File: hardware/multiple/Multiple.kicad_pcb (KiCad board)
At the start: 2 copper layers, 15 x 100 mm, 10 parts, among them J1 AudioJack2_SwitchT, J2 AudioJack2_SwitchT, J3 AudioJack2_SwitchT, J4 AudioJack2_SwitchT, J5 AudioJack2_SwitchT, J6 AudioJack2_SwitchT, J7 AudioJack2_SwitchT, J8 AudioJack2_SwitchT, SW1 SW_Push_DPDT

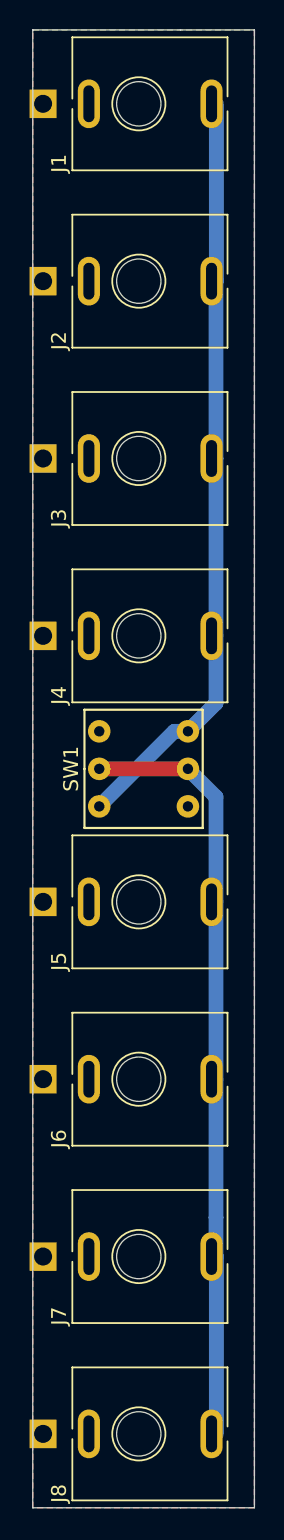
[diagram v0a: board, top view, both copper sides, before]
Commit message: Fix jack centering
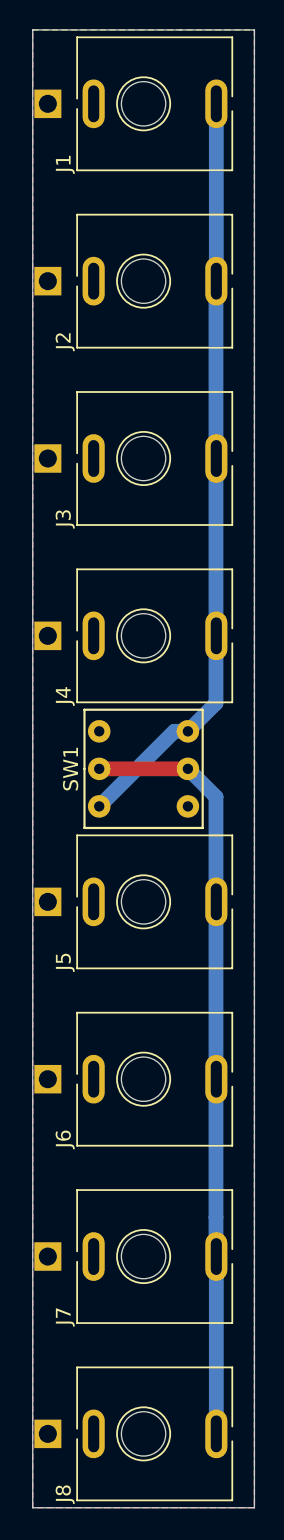
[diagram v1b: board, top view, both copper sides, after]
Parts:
- moved J1 0.32 mm to (151.0, 45.0)
- moved J2 0.32 mm to (151.0, 57.0)
- moved J3 0.32 mm to (151.0, 69.0)
- moved J4 0.32 mm to (151.0, 81.0)
- moved J5 0.32 mm to (151.0, 99.0)
- moved J6 0.32 mm to (151.0, 111.0)
- moved J7 0.32 mm to (151.0, 123.0)
- moved J8 0.32 mm to (151.0, 135.0)
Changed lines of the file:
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@@
 	(footprint "_NTSFootprints:Jack_3.5mm_QingPu_WQP-PJ398SM_Vertical_CenterHole_OvalPads"
 		(layer "F.Cu")
-		(at 150.7 99 90)
+		(at 151.023 99 90)
 		(descr "TRS 3.5mm, vertical, Thonkiconn, PCB mount, (http://www.qingpu-electronics.com/en/products/WQP-PJ398SM-362.html)")
 		(tags "WQP-PJ398SM WQP-PJ301M-12 TRS 3.5mm mono vertical jack thonkiconn qingpu")
@@
 	(footprint "_NTSFootprints:Jack_3.5mm_QingPu_WQP-PJ398SM_Vertical_CenterHole_OvalPads"
 		(layer "F.Cu")
-		(at 150.7 57 90)
+		(at 151.023 57 90)
 		(descr "TRS 3.5mm, vertical, Thonkiconn, PCB mount, (http://www.qingpu-electronics.com/en/products/WQP-PJ398SM-362.html)")
 		(tags "WQP-PJ398SM WQP-PJ301M-12 TRS 3.5mm mono vertical jack thonkiconn qingpu")
@@
 	(footprint "_NTSFootprints:Jack_3.5mm_QingPu_WQP-PJ398SM_Vertical_CenterHole_OvalPads"
 		(layer "F.Cu")
-		(at 150.7 123 90)
+		(at 151.023 123 90)
 		(descr "TRS 3.5mm, vertical, Thonkiconn, PCB mount, (http://www.qingpu-electronics.com/en/products/WQP-PJ398SM-362.html)")
 		(tags "WQP-PJ398SM WQP-PJ301M-12 TRS 3.5mm mono vertical jack thonkiconn qingpu")
@@
 	(footprint "_NTSFootprints:Jack_3.5mm_QingPu_WQP-PJ398SM_Vertical_CenterHole_OvalPads"
 		(layer "F.Cu")
-		(at 150.7 111 90)
+		(at 151.023 111 90)
 		(descr "TRS 3.5mm, vertical, Thonkiconn, PCB mount, (http://www.qingpu-electronics.com/en/products/WQP-PJ398SM-362.html)")
 		(tags "WQP-PJ398SM WQP-PJ301M-12 TRS 3.5mm mono vertical jack thonkiconn qingpu")
@@
 	(footprint "_NTSFootprints:Jack_3.5mm_QingPu_WQP-PJ398SM_Vertical_CenterHole_OvalPads"
 		(layer "F.Cu")
-		(at 150.7 45 90)
+		(at 151.023 45 90)
 		(descr "TRS 3.5mm, vertical, Thonkiconn, PCB mount, (http://www.qingpu-electronics.com/en/products/WQP-PJ398SM-362.html)")
 		(tags "WQP-PJ398SM WQP-PJ301M-12 TRS 3.5mm mono vertical jack thonkiconn qingpu")
@@
 	(footprint "_NTSFootprints:Jack_3.5mm_QingPu_WQP-PJ398SM_Vertical_CenterHole_OvalPads"
 		(layer "F.Cu")
-		(at 150.7 69 90)
+		(at 151.023 69 90)
 		(descr "TRS 3.5mm, vertical, Thonkiconn, PCB mount, (http://www.qingpu-electronics.com/en/products/WQP-PJ398SM-362.html)")
 		(tags "WQP-PJ398SM WQP-PJ301M-12 TRS 3.5mm mono vertical jack thonkiconn qingpu")
@@
 	(footprint "_NTSFootprints:Jack_3.5mm_QingPu_WQP-PJ398SM_Vertical_CenterHole_OvalPads"
 		(layer "F.Cu")
-		(at 150.7 81 90)
+		(at 151.023 81 90)
 		(descr "TRS 3.5mm, vertical, Thonkiconn, PCB mount, (http://www.qingpu-electronics.com/en/products/WQP-PJ398SM-362.html)")
 		(tags "WQP-PJ398SM WQP-PJ301M-12 TRS 3.5mm mono vertical jack thonkiconn qingpu")
@@
 	(footprint "_NTSFootprints:Jack_3.5mm_QingPu_WQP-PJ398SM_Vertical_CenterHole_OvalPads"
 		(layer "F.Cu")
-		(at 150.7 135 90)
+		(at 151.023 135 90)
 		(descr "TRS 3.5mm, vertical, Thonkiconn, PCB mount, (http://www.qingpu-electronics.com/en/products/WQP-PJ398SM-362.html)")
 		(tags "WQP-PJ398SM WQP-PJ301M-12 TRS 3.5mm mono vertical jack thonkiconn qingpu")
